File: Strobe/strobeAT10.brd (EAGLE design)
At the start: 21.3 x 21.3 mm, 11 parts, among them Q2 BC848, U2 ATTINY10-TS8R

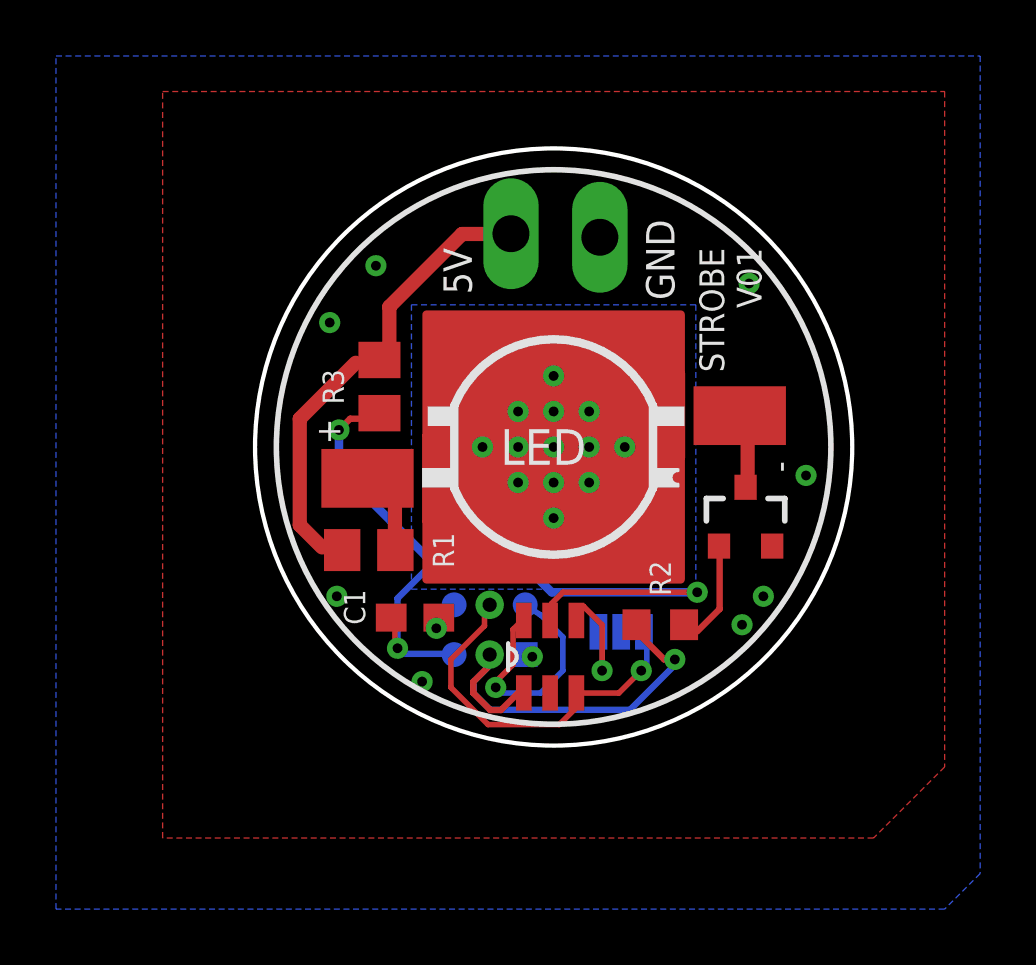
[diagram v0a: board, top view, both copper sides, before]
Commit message: PCB updates (jumper distance) and a new RGB mini board
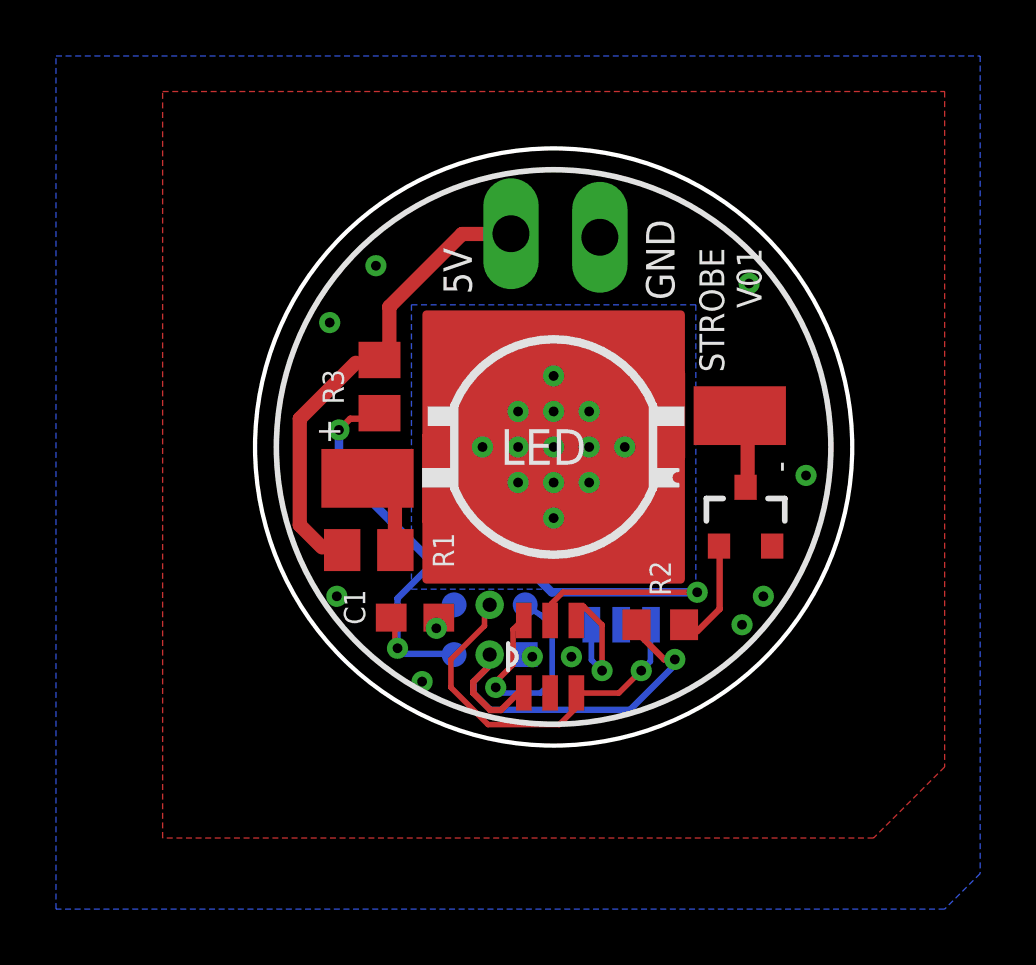
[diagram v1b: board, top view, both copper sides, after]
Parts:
- removed MODE: JUMPER-SMT_3_NO_SILK, SparkFun-Jumpers:SMT-JUMPER_3_NO_SILK
- added JP1: JUMPER-SMT_3_NO_SILK, SparkFun-Jumpers:SMT-JUMPER_3_NO_SILK
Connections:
- net GND: now also JP1.2; no longer MODE.2
- net PB2: now also JP1.3; no longer MODE.1
- net SCK: now also JP1.1; no longer MODE.3
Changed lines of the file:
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@@
 <drawing>
 <settings>
-<setting alwaysvectorfont="no"/>
+<setting alwaysvectorfont="yes"/>
 <setting verticaltext="up"/>
 </settings>
 <grid distance="50" unitdist="mil" unit="mil" style="lines" multiple="1" display="no" altdistance="5" altunitdist="mil" altunit="mil"/>
 <layers>
-<layer number="1" name="Top" color="4" fill="1" visible="yes" active="yes"/>
+<layer number="1" name="Top" color="4" fill="1" visible="no" active="yes"/>
 <layer number="2" name="Route2" color="16" fill="1" visible="no" active="no"/>
 <layer number="3" name="Route3" color="17" fill="1" visible="no" active="no"/>
@@
 <layer number="14" name="Route14" color="22" fill="1" visible="no" active="no"/>
 <layer number="15" name="Route15" color="23" fill="1" visible="no" active="no"/>
-<layer number="16" name="Bottom" color="1" fill="1" visible="no" active="yes"/>
+<layer number="16" name="Bottom" color="1" fill="1" visible="yes" active="yes"/>
 <layer number="17" name="Pads" color="2" fill="1" visible="yes" active="yes"/>
 <layer number="18" name="Vias" color="2" fill="1" visible="yes" active="yes"/>
 <layer number="19" name="Unrouted" color="6" fill="1" visible="yes" active="yes"/>
 <layer number="20" name="Dimension" color="24" fill="1" visible="yes" active="yes"/>
-<layer number="21" name="tPlace" color="7" fill="1" visible="yes" active="yes"/>
-<layer number="22" name="bPlace" color="7" fill="1" visible="no" active="yes"/>
-<layer number="23" name="tOrigins" color="15" fill="1" visible="yes" active="yes"/>
-<layer number="24" name="bOrigins" color="15" fill="1" visible="no" active="yes"/>
-<layer number="25" name="tNames" color="7" fill="1" visible="yes" active="yes"/>
-<layer number="26" name="bNames" color="7" fill="1" visible="no" active="yes"/>
+<layer number="21" name="tPlace" color="7" fill="1" visible="no" active="yes"/>
+<layer number="22" name="bPlace" color="7" fill="1" visible="yes" active="yes"/>
+<layer number="23" name="tOrigins" color="15" fill="1" visible="no" active="yes"/>
+<layer number="24" name="bOrigins" color="15" fill="1" visible="yes" active="yes"/>
+<layer number="25" name="tNames" color="7" fill="1" visible="no" active="yes"/>
+<layer number="26" name="bNames" color="7" fill="1" visible="yes" active="yes"/>
 <layer number="27" name="tValues" color="7" fill="1" visible="no" active="yes"/>
 <layer number="28" name="bValues" color="7" fill="1" visible="no" active="yes"/>
@@
 <layer number="37" name="tTest" color="7" fill="1" visible="no" active="yes"/>
 <layer number="38" name="bTest" color="7" fill="1" visible="no" active="yes"/>
-<layer number="39" name="tKeepout" color="4" fill="11" visible="yes" active="yes"/>
-<layer number="40" name="bKeepout" color="1" fill="11" visible="no" active="yes"/>
-<layer number="41" name="tRestrict" color="4" fill="10" visible="yes" active="yes"/>
-<layer number="42" name="bRestrict" color="1" fill="10" visible="no" active="yes"/>
+<layer number="39" name="tKeepout" color="4" fill="11" visible="no" active="yes"/>
+<layer number="40" name="bKeepout" color="1" fill="11" visible="yes" active="yes"/>
+<layer number="41" name="tRestrict" color="4" fill="10" visible="no" active="yes"/>
+<layer number="42" name="bRestrict" color="1" fill="10" visible="yes" active="yes"/>
 <layer number="43" name="vRestrict" color="2" fill="10" visible="no" active="yes"/>
 <layer number="44" name="Drills" color="7" fill="1" visible="no" active="yes"/>
@@
 <layer number="49" name="Reference" color="7" fill="1" visible="no" active="yes"/>
 <layer number="50" name="dxf" color="7" fill="1" visible="no" active="no"/>
-<layer number="51" name="tDocu" color="7" fill="1" visible="yes" active="yes"/>
-<layer number="52" name="bDocu" color="7" fill="1" visible="no" active="yes"/>
+<layer number="51" name="tDocu" color="7" fill="1" visible="no" active="yes"/>
+<layer number="52" name="bDocu" color="7" fill="1" visible="yes" active="yes"/>
 <layer number="53" name="tGND_GNDA" color="7" fill="9" visible="no" active="no"/>
 <layer number="54" name="bGND_GNDA" color="1" fill="9" visible="no" active="no"/>
@@
 </element>
 <element name="U$1" library="CoreDuino" package="ISCP_PADS_2ROW2HNEW" value="ISCP_PORTPOGONEW" x="-26.416" y="92.1512" smashed="yes" rot="MR180"/>
-<element name="MODE" library="SparkFun-Jumpers" library_urn="urn:adsk.eagle:library:528" package="SMT-JUMPER_3_NO_SILK" package3d_urn="urn:adsk.eagle:package:39285/1" value="JUMPER-SMT_3_NO_SILK" x="-21.717" y="91.186" smashed="yes" rot="MR180">
-<attribute name="NAME" x="-21.717" y="90.043" size="0.6096" layer="26" font="vector" ratio="20" rot="MR180" align="bottom-center"/>
-<attribute name="VALUE" x="-21.717" y="92.329" size="0.6096" layer="28" font="vector" ratio="20" rot="MR180" align="top-center"/>
-</element>
 <element name="R2" library="resistor" library_urn="urn:adsk.eagle:library:348" package="R0603" package3d_urn="urn:adsk.eagle:package:23555/2" value="100R" x="-20.32" y="91.44" smashed="yes" rot="R180">
 <attribute name="NAME" x="-20.701" y="93.726" size="0.762" layer="25" rot="R270"/>
 <attribute name="VALUE" x="-19.685" y="93.98" size="1.27" layer="27" rot="R180"/>
+</element>
+<element name="JP1" library="SparkFun-Jumpers" package="SMT-JUMPER_3_NO_SILK" package3d_urn="urn:adsk.eagle:package:39285/1" value="JUMPER-SMT_3_NO_SILK" x="-21.717" y="91.44" smashed="yes" rot="MR0">
+<attribute name="VALUE" x="-21.717" y="90.297" size="0.6096" layer="28" font="vector" ratio="20" rot="MR0" align="top-center"/>
 </element>
 </elements>
@@
 <vertex x="-41.91" y="81.28"/>
 </polygon>
-<contactref element="MODE" pad="2"/>
 <via x="-31.877" y="92.456" extent="1-16" drill="0.35"/>
 <via x="-28.829" y="89.408" extent="1-16" drill="0.35"/>
@@
 <via x="-30.48" y="104.267" extent="1-16" drill="0.35"/>
 <via x="-32.131" y="102.235" extent="1-16" drill="0.35"/>
+<contactref element="JP1" pad="2"/>
+<via x="-23.495" y="90.297" extent="1-16" drill="0.35"/>
 </signal>
 <signal name="SCK">
@@
 <contactref element="U$1" pad="SC"/>
 <contactref element="U$1" pad="SCK"/>
-<contactref element="MODE" pad="3"/>
 <wire x1="-21.8" y1="89" x2="-23.2" y2="89" width="0.2" layer="1"/>
 <wire x1="-21" y1="89.8" x2="-21.8" y2="89" width="0.2" layer="1"/>
-<wire x1="-20.8" y1="90" x2="-21" y2="89.8" width="0.2" layer="16"/>
-<wire x1="-20.8" y1="91" x2="-20.8" y2="90" width="0.2" layer="16"/>
+<wire x1="-20.673" y1="90.127" x2="-21" y2="89.8" width="0.2" layer="16"/>
+<wire x1="-20.673" y1="91" x2="-20.673" y2="90.127" width="0.2" layer="16"/>
 <wire x1="-23.2" y1="89" x2="-23.3172" y2="89.0016" width="0.2" layer="1"/>
-<wire x1="-20.8" y1="91" x2="-20.9042" y2="91.186" width="0.2" layer="16"/>
 <wire x1="-26.6" y1="91.4" x2="-26.6" y2="92.054" width="0.2" layer="1"/>
 <wire x1="-27.8" y1="90.2" x2="-26.6" y2="91.4" width="0.2" layer="1"/>
@@
 <wire x1="-23.4" y1="89" x2="-23.3172" y2="89.0016" width="0.2" layer="1"/>
 <via x="-21" y="89.8" extent="1-16" drill="0.35"/>
+<contactref element="JP1" pad="1"/>
+<wire x1="-20.6502" y1="91.44" x2="-20.6502" y2="91.0228" width="0.2" layer="16"/>
+<wire x1="-20.6502" y1="91.0228" x2="-20.673" y2="91" width="0.2" layer="16"/>
 </signal>
 <signal name="MO">
@@
 <contactref element="U$1" pad="RST"/>
 <wire x1="-24.6" y1="91.8" x2="-24.618478125" y2="91.8" width="0.2" layer="16"/>
-<wire x1="-23.8" y1="91" x2="-24.6" y2="91.8" width="0.2" layer="16"/>
-<wire x1="-23.8" y1="89.8" x2="-23.8" y2="91" width="0.2" layer="16"/>
-<wire x1="-24.6" y1="89" x2="-23.8" y2="89.8" width="0.2" layer="16"/>
+<wire x1="-24.181" y1="91.381" x2="-24.6" y2="91.8" width="0.2" layer="16"/>
+<wire x1="-24.181" y1="89.419" x2="-24.181" y2="91.381" width="0.2" layer="16"/>
+<wire x1="-24.6" y1="89" x2="-24.181" y2="89.419" width="0.2" layer="16"/>
 <wire x1="-26" y1="89" x2="-24.6" y2="89" width="0.2" layer="16"/>
 <wire x1="-26.2" y1="89.2" x2="-26" y2="89" width="0.2" layer="16"/>
@@
 <signal name="PB2">
 <contactref element="U2" pad="4"/>
-<contactref element="MODE" pad="1"/>
-<wire x1="-22.4" y1="89.8" x2="-22.4" y2="91" width="0.2" layer="16"/>
+<wire x1="-22.781" y1="91.4372" x2="-22.781" y2="90.181" width="0.2" layer="16"/>
+<wire x1="-22.4" y1="89.8" x2="-22.781" y2="90.181" width="0.2" layer="16"/>
 <wire x1="-22.4" y1="91.435" x2="-22.4" y2="89.8" width="0.2" layer="1"/>
 <wire x1="-23.0635" y1="92.0985" x2="-22.4" y2="91.435" width="0.2" layer="1"/>
 <wire x1="-23.0635" y1="92.0985" x2="-23.3172" y2="91.8448" width="0.2" layer="1"/>
 <wire x1="-23.3172" y1="91.5924" x2="-23.3172" y2="91.8448" width="0.2" layer="1"/>
-<wire x1="-22.4" y1="91" x2="-22.5298" y2="91.186" width="0.2" layer="16"/>
 <via x="-22.4" y="89.8" extent="1-16" drill="0.35"/>
+<contactref element="JP1" pad="3"/>
+<wire x1="-22.781" y1="91.4372" x2="-22.7838" y2="91.44" width="0.2" layer="16"/>
 </signal>
 <signal name="N$1">
